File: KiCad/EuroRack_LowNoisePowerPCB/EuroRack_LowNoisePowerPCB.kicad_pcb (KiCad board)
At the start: 2 copper layers, 188 x 48.3 mm, 38 parts, among them J1 Conn_01x04, J2 Conn_01x03_Male, J3 Conn_02x08_Odd_Even, J4 Conn_02x08_Odd_Even, J5 Conn_02x08_Odd_Even, U1 LM7805_TO220

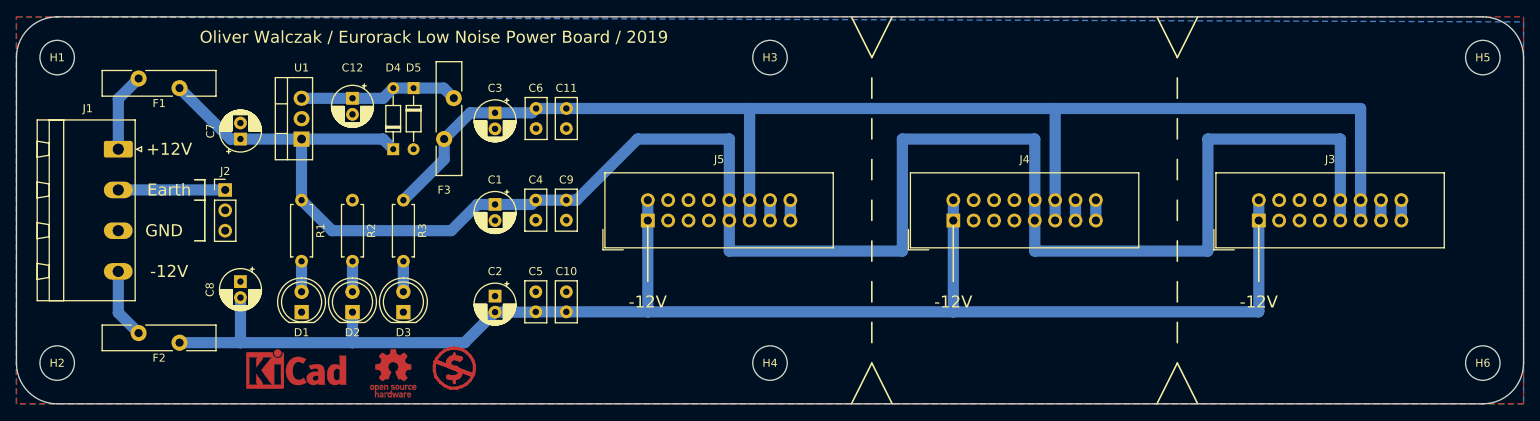
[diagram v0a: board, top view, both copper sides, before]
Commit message: Migrate to KiCad 7 Remove PTC and remove grounding option
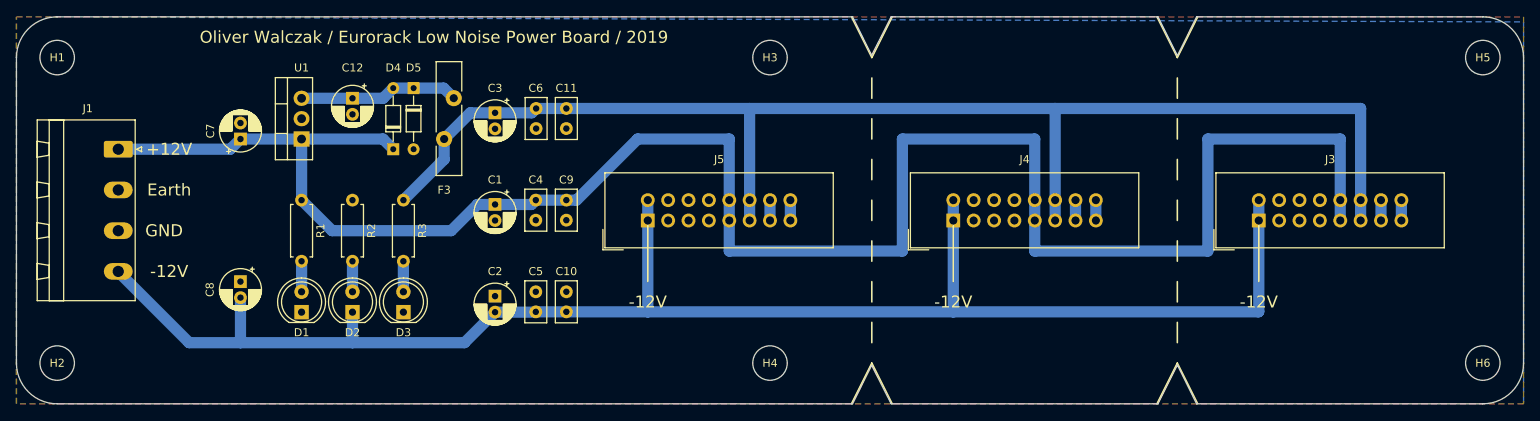
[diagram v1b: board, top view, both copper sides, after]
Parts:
- removed F1, F2: MF-RX160/72-0, Fuse:Fuse_Bourns_MF-RG900
- removed J2: Conn_01x03_Male, Connector_PinHeader_2.54mm:PinHeader_1x03_P2.54mm_Vertical
- removed REF**: Symbol_CC-Noncommercial_CopperTop_Small, Symbol:Symbol_CC-Noncommercial_CopperTop_Small
- removed REF**: OSHW-Logo_5.7x6mm_Copper, Symbol:OSHW-Logo_5.7x6mm_Copper
- removed REF**: KiCad-Logo_5mm_Copper, Symbol:KiCad-Logo_5mm_Copper
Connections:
- C1 pad 1: /+12V -> VCC
- C10 pad 2: /-12V -> VEE
- C2 pad 2: /-12V -> VEE
- C4 pad 1: /+12V -> VCC
- C5 pad 2: /-12V -> VEE
- C7 pad 1: /+12V -> VCC
- C8 pad 2: /-12V -> VEE
- C9 pad 1: /+12V -> VCC
- D2 pad 1: /-12V -> VEE
- D4 pad 1: /+12V -> VCC
- J1 pad 2: /EARTH -> GND
- J3 pad 1: /-12V -> VEE
- J3 pad 10: /+12V -> VCC
- J3 pad 2: /-12V -> VEE
- J3 pad 9: /+12V -> VCC
- J4 pad 1: /-12V -> VEE
- J4 pad 10: /+12V -> VCC
- J4 pad 2: /-12V -> VEE
- J4 pad 9: /+12V -> VCC
- J5 pad 1: /-12V -> VEE
- J5 pad 10: /+12V -> VCC
- J5 pad 2: /-12V -> VEE
- J5 pad 9: /+12V -> VCC
- R1 pad 1: /+12V -> VCC
- U1 pad 1: /+12V -> VCC
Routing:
- net /+12V: track 239.3 -> 0.00 mm
- net VCC: track 9.87 -> 244.9 mm
- net VEE: track 8.74 -> 198.7 mm
- net /-12V: track 187.4 -> 0.00 mm
- net /EARTH: track 13.3 -> 0.00 mm
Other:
- outline, holes or cut-outs redrawn
- net class Default removed
